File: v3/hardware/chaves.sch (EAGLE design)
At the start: 93 parts, among them IC1 40106N, J2 DCJ0202, T1 bc547, T2 bc547

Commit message: changing pinheaders to connect the trigger in properly
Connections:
- removed net N$20: C4.1, C5.1, IC1B.I, R1.1
- removed net N$21: C6.1, C7.1, IC1C.I, R2.1
- removed net N$31: C1.1, C2.1, IC1A.I, R5.2
- removed net N$35: C8.1, C9.1, IC1D.I, R3.1
- removed net N$36: C10.1, C11.1, IC1E.I, R4.1
- removed net N$54: C12.1, C13.1, IC1F.I, R8.2
- new net GNDA: U$1.P, U$2.P, U$3.P, U$4.P, U$5.P, U$6.P
- net SS1: now also C1.1, C2.1, IC1A.I, R5.2; no longer U$1.P
- net SS2: now also C4.1, C5.1, IC1B.I, R1.1; no longer U$2.P
- net SS3: now also C6.1, C7.1, IC1C.I, R2.1; no longer U$3.P
- net SS4: now also C8.1, C9.1, IC1D.I, R3.1; no longer U$4.P
- net SS5: now also C10.1, C11.1, IC1E.I, R4.1; no longer U$5.P
- net SS6: now also C12.1, C13.1, IC1F.I, R8.2; no longer U$6.P
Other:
- moved on the sheet: U$2, U$3

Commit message: Finixhed position and merged pins
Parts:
- removed IN1, IN2, IN3: (no value), adafruit:PINHD-1X3CB
- removed VCO1, VCO2, VCO3, VCO4, VCO5, VCO6: 1X4-CLEANBIG, adafruit:1X4-CLEANBIG
- added JP1: (no value), adafruit:PINHD-1X9
- added O13, O45: (no value), adafruit:PINHD-1X12-CB
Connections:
- net VCC renamed VIN
- removed net N$14: GJ.1, GREEN.1, GREEN.2, GREEN.3, GREEN.4, GREEN.5, GREEN.6
- removed net N$15: BJ.1, BLUE.1, BLUE.2, BLUE.3, BLUE.4, BLUE.5, BLUE.6
- removed net N$18: U$7.P, VCO1.1, VCO1.2, VCO1.3, VCO1.4
- removed net N$25: IN1.1, IN1.2, IN1.3, JIN1.TIP
- removed net N$27: U$8.P, VCO2.1, VCO2.2, VCO2.3, VCO2.4
- removed net N$30: U$9.P, VCO3.1, VCO3.2, VCO3.3, VCO3.4
- removed net N$39: U$10.P, VCO4.1, VCO4.2, VCO4.3, VCO4.4
- removed net N$42: U$11.P, VCO6.1, VCO6.2, VCO6.3, VCO6.4
- removed net N$45: U$12.P, VCO5.1, VCO5.2, VCO5.3, VCO5.4
- new net BOUT: BJ.1, BLUE.1, BLUE.2, BLUE.3, BLUE.4, BLUE.5, BLUE.6, JP1.7
- new net GOUT: GJ.1, GREEN.1, GREEN.2, GREEN.3, GREEN.4, GREEN.5, GREEN.6, JP1.4
- new net N$20: JP8.2, JP8.4, JP8.6, U$1.P
- new net N$23: JP9.2, JP9.4, JP9.6, U$3.P
- new net N$31: JP10.2, JP10.4, JP10.6, U$4.P
- new net N$35: JP11.2, JP11.4, JP11.6, U$5.P
- new net N$36: JP12.2, JP12.4, JP12.6, U$6.P
- new net OUT1: O13.1, O13.2, O13.3, O13.4, U$7.P
- new net OUT2: O13.5, O13.6, O13.7, O13.8, U$8.P
- new net OUT3: O13.10, O13.11, O13.12, O13.9, U$9.P
- new net OUT4: O45.1, O45.2, O45.3, O45.4, U$10.P
- new net OUT5: O45.5, O45.6, O45.7, O45.8, U$11.P
- new net OUT6: O45.10, O45.11, O45.12, O45.9, U$12.P
- new net ROUT: JP1.1, RED.1, RED.2, RED.3, RED.4, RED.5, RED.6, RJ.1
- net GND: no longer JP10.3, JP11.3, JP12.3, JP3.3, JP8.3, JP9.3
- net GNDA: now also JP10.3, JP11.3, JP12.3, JP8.3, JP9.3; no longer U$1.P, U$3.P, U$4.P, U$5.P, U$6.P
- net N$12: now also JIN2.TIP, JP1.5, JP1.6; no longer IN3.1, IN3.2, IN3.3, JIN3.TIP
- net N$13: now also JIN3.TIP, JP1.8, JP1.9; no longer RED.1, RED.2, RED.3, RED.4, RED.5, RED.6, RJ.1
- net N$9: now also JIN1.TIP, JP1.2, JP1.3; no longer IN2.1, IN2.2, IN2.3, JIN2.TIP
- net SS1: no longer JP8.2, JP8.4, JP8.6
- net SS3: no longer JP9.2, JP9.4, JP9.6
- net SS4: no longer JP10.2, JP10.4, JP10.6
- net SS5: no longer JP11.2, JP11.4, JP11.6
- net SS6: no longer JP12.2, JP12.4, JP12.6
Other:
- moved on the sheet: U$6

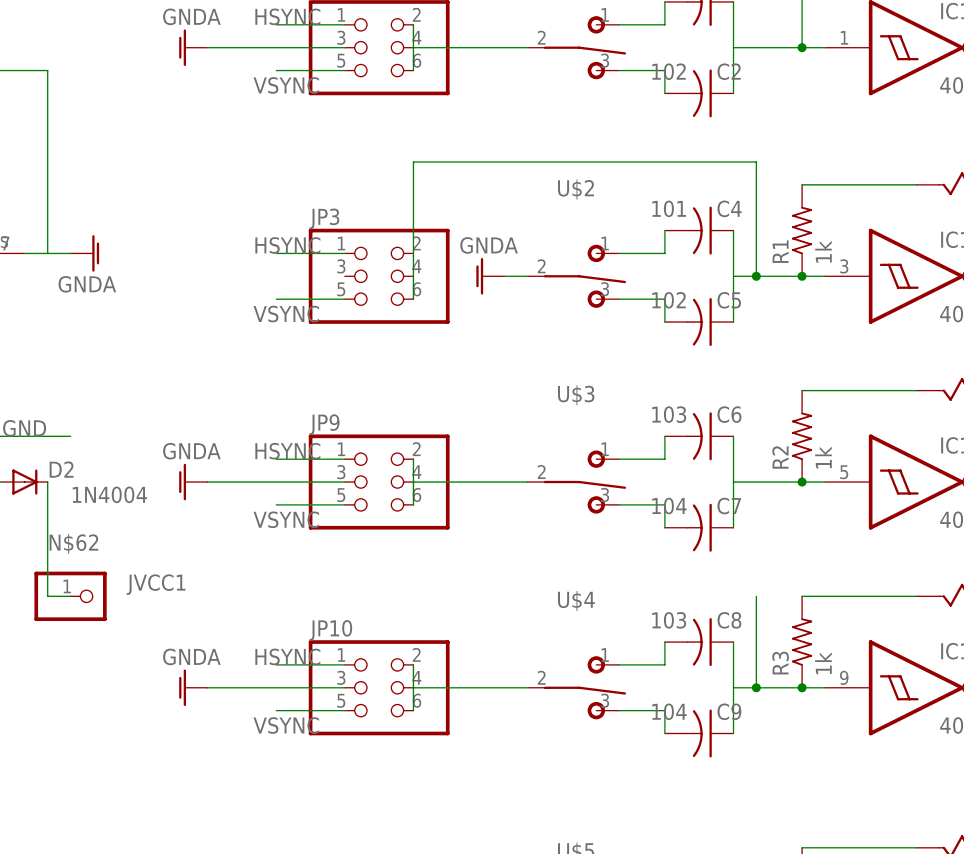
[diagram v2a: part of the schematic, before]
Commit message: fully routed v3, checked errors, layers corrected ready to fav proto
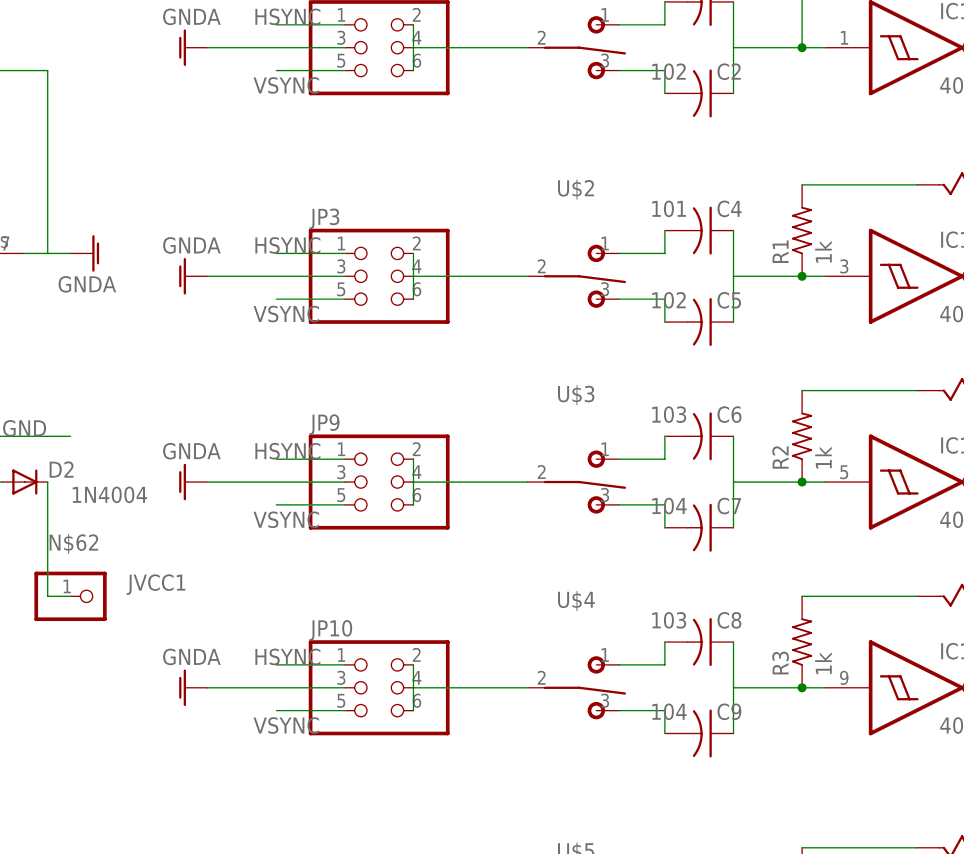
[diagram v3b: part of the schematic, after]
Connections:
- removed net GNDA: JP10.3, JP11.3, JP12.3, JP8.3, JP9.3, U$2.P
- new net N$14: JP3.2, JP3.4, JP3.6, U$2.P
- net GND: now also JP10.3, JP11.3, JP12.3, JP3.3, JP8.3, JP9.3
- net SS2: no longer JP3.2, JP3.4, JP3.6
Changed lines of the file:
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@@
 <instance part="JIN3" gate="G$1" x="218.44" y="66.04"/>
 <instance part="GND4" gate="1" x="-43.18" y="142.24" rot="R270"/>
-<instance part="GND9" gate="1" x="-10.16" y="116.84" rot="R270"/>
+<instance part="GND9" gate="1" x="-43.18" y="116.84" rot="R270"/>
 <instance part="GND10" gate="1" x="-43.18" y="93.98" rot="R270"/>
 <instance part="GND11" gate="1" x="-43.18" y="71.12" rot="R270"/>
@@
 <net name="SS2" class="0">
 <segment>
-<pinref part="JP3" gate="A" pin="4"/>
-<pinref part="JP3" gate="A" pin="2"/>
-<wire x1="-17.78" y1="119.38" x2="-17.78" y2="116.84" width="0.1524" layer="91"/>
-<pinref part="JP3" gate="A" pin="6"/>
-<wire x1="-17.78" y1="116.84" x2="-17.78" y2="114.3" width="0.1524" layer="91"/>
-<wire x1="-17.78" y1="119.38" x2="-17.78" y2="129.54" width="0.1524" layer="91"/>
-<wire x1="-17.78" y1="129.54" x2="20.32" y2="129.54" width="0.1524" layer="91"/>
 <pinref part="C5" gate="G$1" pin="1"/>
 <pinref part="C4" gate="G$1" pin="1"/>
@@
 <pinref part="R1" gate="G$1" pin="1"/>
 <junction x="25.4" y="116.84"/>
-<wire x1="25.4" y1="116.84" x2="20.32" y2="116.84" width="0.1524" layer="91"/>
-<wire x1="20.32" y1="116.84" x2="17.78" y2="116.84" width="0.1524" layer="91"/>
+<wire x1="25.4" y1="116.84" x2="17.78" y2="116.84" width="0.1524" layer="91"/>
 <wire x1="17.78" y1="116.84" x2="17.78" y2="111.76" width="0.1524" layer="91"/>
-<wire x1="20.32" y1="129.54" x2="20.32" y2="116.84" width="0.1524" layer="91"/>
-<junction x="20.32" y="116.84"/>
 </segment>
 </net>
@@
 <wire x1="27.94" y1="71.12" x2="25.4" y2="71.12" width="0.1524" layer="91"/>
 <pinref part="C9" gate="G$1" pin="1"/>
-<wire x1="25.4" y1="71.12" x2="20.32" y2="71.12" width="0.1524" layer="91"/>
-<wire x1="20.32" y1="71.12" x2="17.78" y2="71.12" width="0.1524" layer="91"/>
+<wire x1="25.4" y1="71.12" x2="17.78" y2="71.12" width="0.1524" layer="91"/>
 <wire x1="17.78" y1="66.04" x2="17.78" y2="71.12" width="0.1524" layer="91"/>
 <pinref part="R3" gate="G$1" pin="1"/>
 <junction x="25.4" y="71.12"/>
-<wire x1="20.32" y1="81.28" x2="20.32" y2="71.12" width="0.1524" layer="91"/>
-<junction x="20.32" y="71.12"/>
 </segment>
 </net>
@@
 <wire x1="210.82" y1="63.5" x2="213.36" y2="63.5" width="0.1524" layer="91"/>
 <pinref part="JIN3" gate="G$1" pin="SLEEVE"/>
+</segment>
+<segment>
+<pinref part="JP12" gate="A" pin="3"/>
+<pinref part="GND13" gate="1" pin="GNDA"/>
+<wire x1="-40.64" y1="7.62" x2="-25.4" y2="7.62" width="0.1524" layer="91"/>
+</segment>
+<segment>
+<pinref part="JP11" gate="A" pin="3"/>
+<pinref part="GND12" gate="1" pin="GNDA"/>
+<wire x1="-40.64" y1="43.18" x2="-25.4" y2="43.18" width="0.1524" layer="91"/>
+</segment>
+<segment>
+<pinref part="JP10" gate="A" pin="3"/>
+<pinref part="GND11" gate="1" pin="GNDA"/>
+<wire x1="-40.64" y1="71.12" x2="-25.4" y2="71.12" width="0.1524" layer="91"/>
+</segment>
+<segment>
+<pinref part="JP9" gate="A" pin="3"/>
+<pinref part="GND10" gate="1" pin="GNDA"/>
+<wire x1="-40.64" y1="93.98" x2="-25.4" y2="93.98" width="0.1524" layer="91"/>
+</segment>
+<segment>
+<pinref part="JP8" gate="A" pin="3"/>
+<pinref part="GND4" gate="1" pin="GNDA"/>
+<wire x1="-40.64" y1="142.24" x2="-25.4" y2="142.24" width="0.1524" layer="91"/>
+</segment>
+<segment>
+<pinref part="JP3" gate="A" pin="3"/>
+<pinref part="GND9" gate="1" pin="GNDA"/>
+<wire x1="-40.64" y1="116.84" x2="-25.4" y2="116.84" width="0.1524" layer="91"/>
 </segment>
 </net>
@@
 </segment>
 </net>
-<net name="GNDA" class="0">
-<segment>
-<pinref part="JP12" gate="A" pin="3"/>
-<pinref part="GND13" gate="1" pin="GNDA"/>
-<wire x1="-40.64" y1="7.62" x2="-25.4" y2="7.62" width="0.1524" layer="91"/>
-</segment>
-<segment>
-<pinref part="JP11" gate="A" pin="3"/>
-<pinref part="GND12" gate="1" pin="GNDA"/>
-<wire x1="-40.64" y1="43.18" x2="-25.4" y2="43.18" width="0.1524" layer="91"/>
-</segment>
-<segment>
-<pinref part="JP10" gate="A" pin="3"/>
-<pinref part="GND11" gate="1" pin="GNDA"/>
-<wire x1="-40.64" y1="71.12" x2="-25.4" y2="71.12" width="0.1524" layer="91"/>
-</segment>
-<segment>
-<pinref part="JP9" gate="A" pin="3"/>
-<pinref part="GND10" gate="1" pin="GNDA"/>
-<wire x1="-40.64" y1="93.98" x2="-25.4" y2="93.98" width="0.1524" layer="91"/>
-</segment>
-<segment>
-<pinref part="JP8" gate="A" pin="3"/>
-<pinref part="GND4" gate="1" pin="GNDA"/>
-<wire x1="-40.64" y1="142.24" x2="-25.4" y2="142.24" width="0.1524" layer="91"/>
-</segment>
-<segment>
-<pinref part="U$2" gate="G$1" pin="P"/>
-<pinref part="GND9" gate="1" pin="GNDA"/>
-<wire x1="-7.62" y1="116.84" x2="-5.08" y2="116.84" width="0.1524" layer="91"/>
-</segment>
-</net>
 <net name="N$20" class="0">
 <segment>
@@
 </segment>
 </net>
+<net name="N$14" class="0">
+<segment>
+<pinref part="JP3" gate="A" pin="6"/>
+<pinref part="JP3" gate="A" pin="4"/>
+<pinref part="JP3" gate="A" pin="2"/>
+<wire x1="-17.78" y1="119.38" x2="-17.78" y2="116.84" width="0.1524" layer="91"/>
+<wire x1="-17.78" y1="116.84" x2="-17.78" y2="114.3" width="0.1524" layer="91"/>
+<pinref part="U$2" gate="G$1" pin="P"/>
+<wire x1="-17.78" y1="116.84" x2="-5.08" y2="116.84" width="0.1524" layer="91"/>
+</segment>
+</net>

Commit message: Revised gerbers for all versions
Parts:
- removed J2: DCJ0202, con-jack:DCJ0202
- added CN1: (no value), adafruit:DCBARRELPTH
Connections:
- net GND: now also CN1.GND; no longer J2.1
- net VIN: now also CN1.PWR; no longer J2.3
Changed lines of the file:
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@@
 <part name="LED2" library="adafruit" deviceset="LED" device="5MM"/>
 <part name="JIN1" library="pj302m" deviceset="PJ302M" device=""/>
-<part name="J2" library="con-jack" deviceset="DCJ0202" device=""/>
 <part name="D2" library="diode" deviceset="1N4004" device=""/>
 <part name="JVCC1" library="adafruit" deviceset="PINHD-1X1" device=""/>
@@
 <part name="O45" library="adafruit" deviceset="PINHD-1X12" device="-CB"/>
 <part name="JP1" library="adafruit" deviceset="PINHD-1X9" device=""/>
+<part name="CN1" library="adafruit" deviceset="DCBARREL" device="PTH"/>
 </parts>
 <sheets>
@@
 <instance part="LED2" gate="G$1" x="5.08" y="-33.02" rot="MR270"/>
 <instance part="JIN1" gate="G$1" x="218.44" y="116.84"/>
-<instance part="J2" gate="G$1" x="-76.2" y="96.52"/>
 <instance part="D2" gate="1" x="-60.96" y="93.98" smashed="yes">
 <attribute name="NAME" x="-58.42" y="94.4626" size="1.778" layer="95"/>
@@
 <instance part="O45" gate="G$1" x="147.32" y="78.74" rot="R270"/>
 <instance part="JP1" gate="G$1" x="177.8" y="86.36" rot="MR0"/>
+<instance part="CN1" gate="G$1" x="-76.2" y="96.52" rot="MR180"/>
 </instances>
 <busses>
@@
 </segment>
 <segment>
-<pinref part="J2" gate="G$1" pin="1"/>
-<wire x1="-68.58" y1="99.06" x2="-55.88" y2="99.06" width="0.1524" layer="91"/>
+<wire x1="-73.66" y1="99.06" x2="-55.88" y2="99.06" width="0.1524" layer="91"/>
 <label x="-63.5" y="99.06" size="1.778" layer="95"/>
+<pinref part="CN1" gate="G$1" pin="GND"/>
 </segment>
 <segment>
@@
 <net name="VIN" class="0">
 <segment>
-<pinref part="J2" gate="G$1" pin="3"/>
 <pinref part="D2" gate="1" pin="A"/>
-<wire x1="-68.58" y1="93.98" x2="-63.5" y2="93.98" width="0.1524" layer="91"/>
-</segment>
-</net>
+<wire x1="-73.66" y1="93.98" x2="-63.5" y2="93.98" width="0.1524" layer="91"/>
+<pinref part="CN1" gate="G$1" pin="PWR"/>
+</segment>
+</net>
